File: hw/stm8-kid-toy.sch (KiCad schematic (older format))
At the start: 12 parts, among them SW1 SW_Push, SW2 SW_Push, SW3 SW_Push

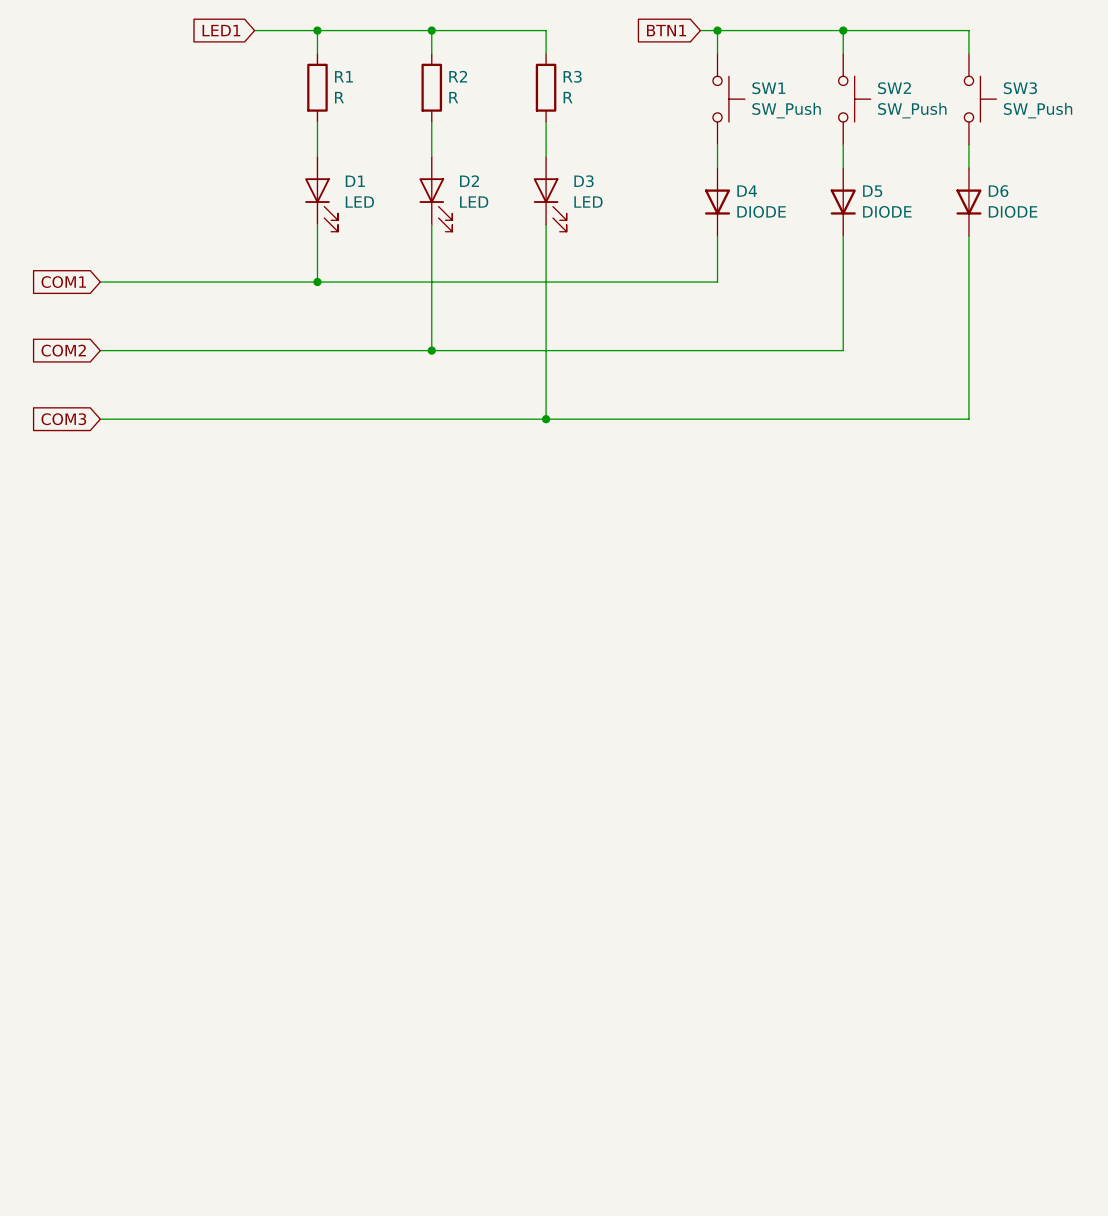
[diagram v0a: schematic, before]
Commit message: Add MCU to schematics
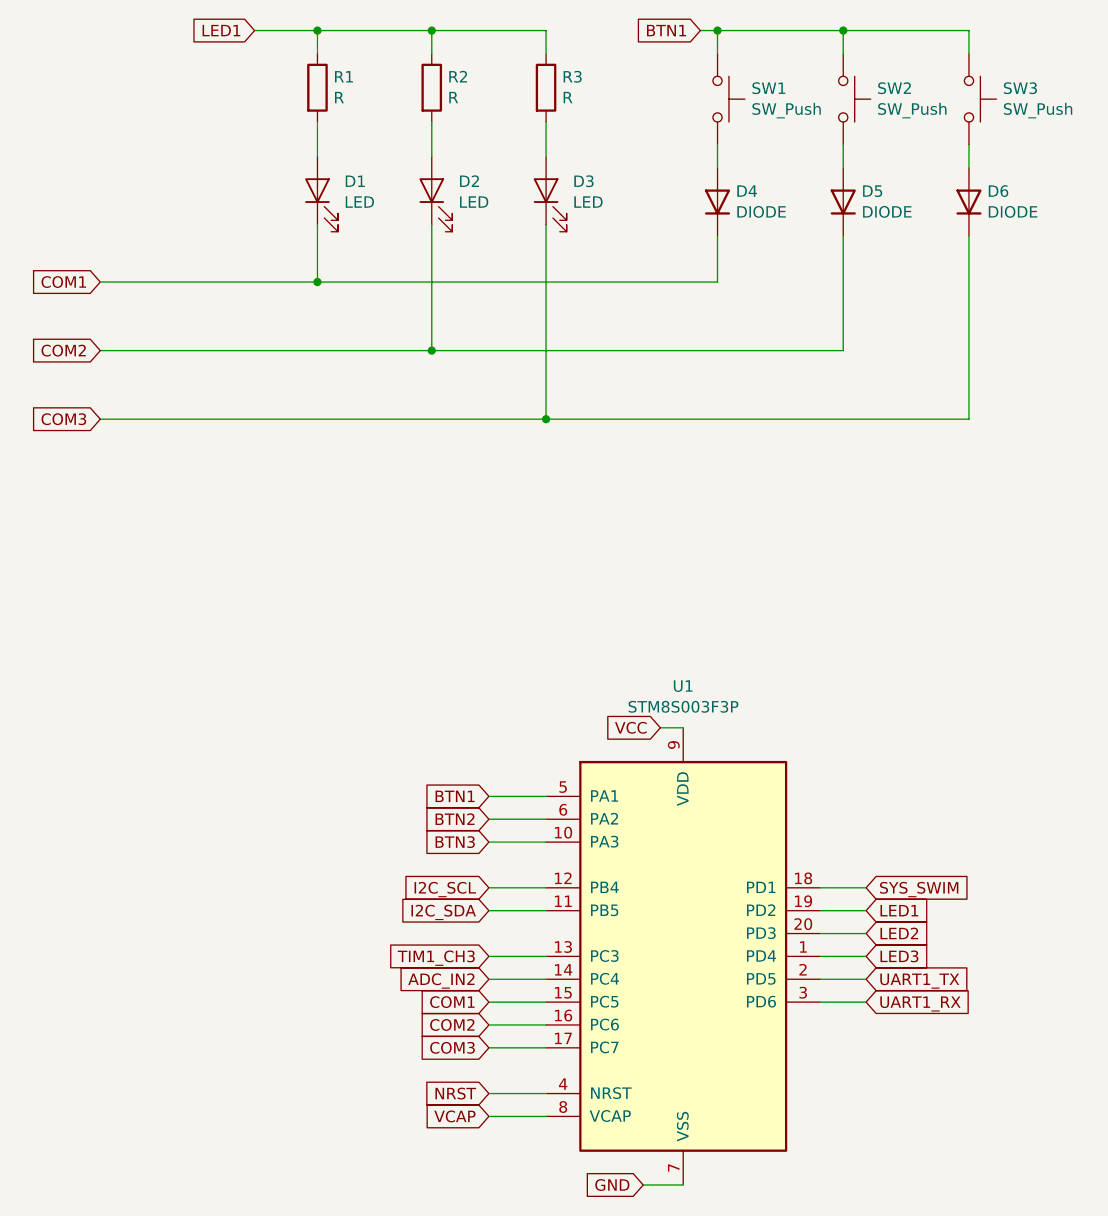
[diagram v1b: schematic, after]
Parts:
- added U1: STM8S003F3P, Package_SO:TSSOP-20_4.4x6.5mm_P0.65mm, symbol MCU_ST_STM8:STM8S003F3P
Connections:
- net BTN1: now also U1.5 (PA1)
- net COM1: now also U1.15 (PC5)
- net COM2: now also U1.16 (PC6)
- net COM3: now also U1.17 (PC7)
- net LED1: now also U1.19 (PD2)
- new net ADC_IN2: U1.14 (PC4)
- new net BTN2: U1.6 (PA2)
- new net BTN3: U1.10 (PA3)
- new net GND: U1.7 (VSS)
- new net I2C_SCL: U1.12 (PB4)
- new net I2C_SDA: U1.11 (PB5)
- new net LED2: U1.20 (PD3)
- new net LED3: U1.1 (PD4)
- new net NRST: U1.4 (NRST)
- new net SYS_SWIM: U1.18 (PD1)
- new net TIM1_CH3: U1.13 (PC3)
- new net UART1_RX: U1.3 (PD6)
- new net UART1_TX: U1.2 (PD5)
- new net VCAP: U1.8 (VCAP)
- new net VCC: U1.9 (VDD)
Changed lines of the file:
@@
 	0    1    1    0
 $EndComp
+$Comp
+L MCU_ST_STM8:STM8S003F3P U1
+U 1 1 5D99B248
+P 3600 5450
+F 0 "U1" H 3600 6631 50  0000 C CNN
+F 1 "STM8S003F3P" H 3600 6540 50  0000 C CNN
+F 2 "Package_SO:TSSOP-20_4.4x6.5mm_P0.65mm" H 3650 6550 50  0001 L CNN
+F 3 "http://www.st.com/st-web-ui/static/active/en/resource/technical/document/datasheet/DM00024550.pdf" H 3550 5050 50  0001 C CNN
+	1    3600 5450
+	1    0    0    -1
+$EndComp
+Text GLabel 2750 4750 0    50   Input ~ 0
+BTN1
+Text GLabel 2750 4850 0    50   Input ~ 0
+BTN2
+Text GLabel 2750 4950 0    50   Input ~ 0
+BTN3
+Wire Wire Line
+	2750 4750 3000 4750
+Wire Wire Line
+	2750 4850 3000 4850
+Wire Wire Line
+	2750 4950 3000 4950
+Text GLabel 2750 5150 0    50   Input ~ 0
+I2C_SCL
+Text GLabel 2750 5250 0    50   Input ~ 0
+I2C_SDA
+Wire Wire Line
+	2750 5150 3000 5150
+Wire Wire Line
+	2750 5250 3000 5250
+Text GLabel 2750 5450 0    50   Input ~ 0
+TIM1_CH3
+Text GLabel 2750 5550 0    50   Input ~ 0
+ADC_IN2
+Text GLabel 2750 5650 0    50   Input ~ 0
+COM1
+Text GLabel 2750 5750 0    50   Input ~ 0
+COM2
+Text GLabel 2750 5850 0    50   Input ~ 0
+COM3
+Text GLabel 2750 6050 0    50   Input ~ 0
+NRST
+Wire Wire Line
+	2750 5450 3000 5450
+Wire Wire Line
+	2750 5550 3000 5550
+Wire Wire Line
+	2750 5650 3000 5650
+Wire Wire Line
+	2750 5750 3000 5750
+Wire Wire Line
+	2750 5850 3000 5850
+Wire Wire Line
+	2750 6050 3000 6050
+Text GLabel 2750 6150 0    50   Input ~ 0
+VCAP
+Wire Wire Line
+	2750 6150 3000 6150
+Text GLabel 3500 4450 0    50   Input ~ 0
+VCC
+Wire Wire Line
+	3500 4450 3600 4450
+Text GLabel 3425 6450 0    50   Input ~ 0
+GND
+Wire Wire Line
+	3425 6450 3600 6450
+Text GLabel 4400 5150 2    50   Input ~ 0
+SYS_SWIM
+Text GLabel 4400 5250 2    50   Input ~ 0
+LED1
+Text GLabel 4400 5350 2    50   Input ~ 0
+LED2
+Text GLabel 4400 5450 2    50   Input ~ 0
+LED3
+Text GLabel 4400 5550 2    50   Input ~ 0
+UART1_TX
+Text GLabel 4400 5650 2    50   Input ~ 0
+UART1_RX
+Wire Wire Line
+	4200 5150 4400 5150
+Wire Wire Line
+	4200 5250 4400 5250
+Wire Wire Line
+	4400 5350 4200 5350
+Wire Wire Line
+	4200 5450 4400 5450
+Wire Wire Line
+	4400 5550 4200 5550
+Wire Wire Line
+	4200 5650 4400 5650
 $EndSCHEMATC
